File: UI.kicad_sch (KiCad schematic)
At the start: 40 parts

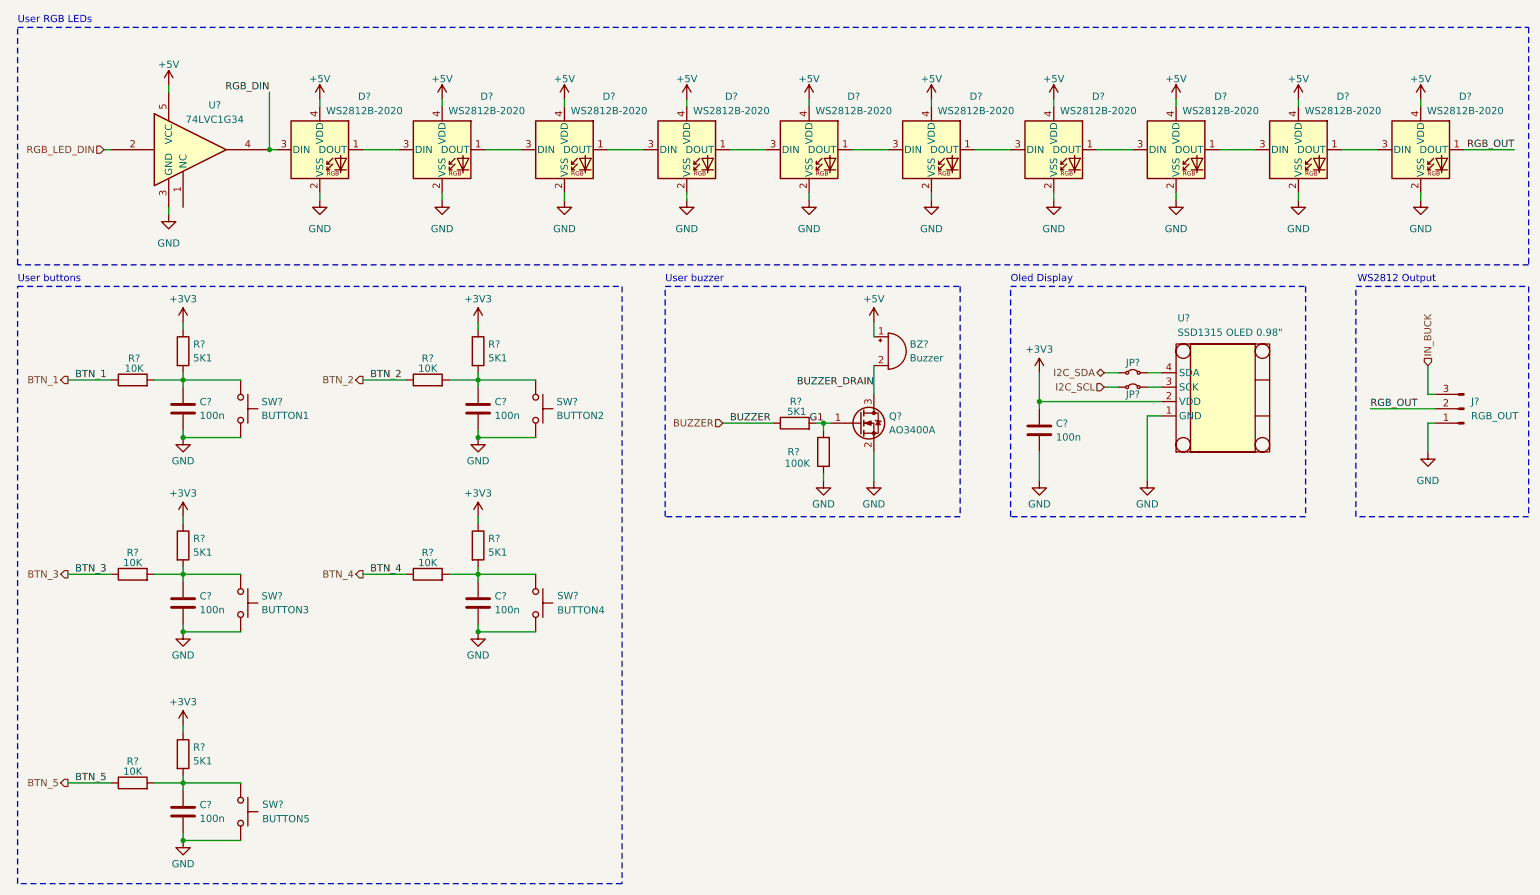
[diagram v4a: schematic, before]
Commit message: Referenced the shematic and started the sourcing part
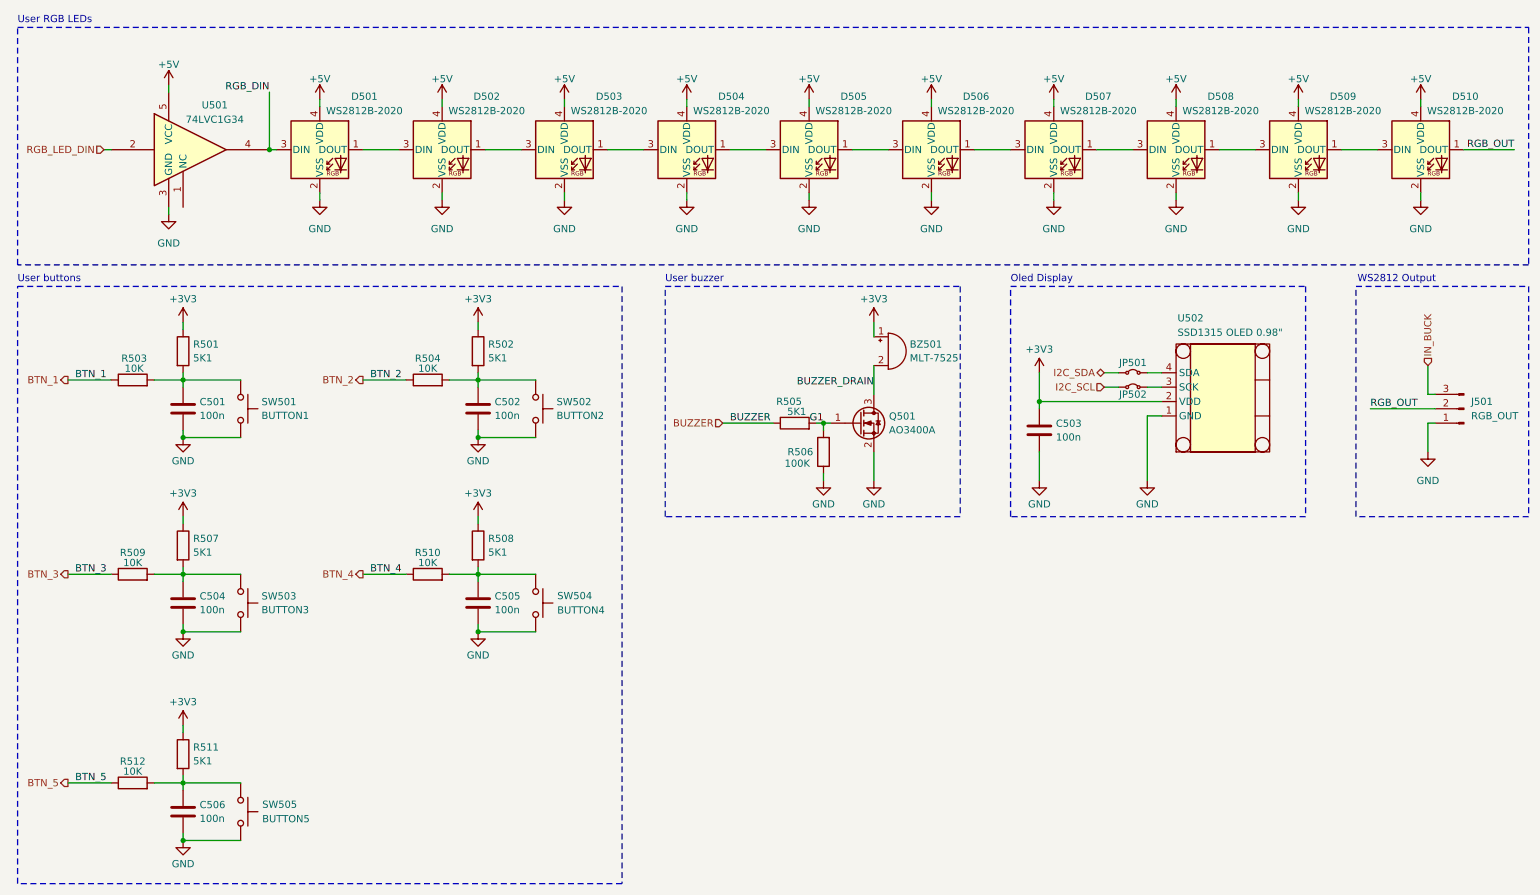
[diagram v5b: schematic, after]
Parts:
- BZ501: renamed from BZ?; value Buzzer -> MLT-7525; footprint Buzzer_Beeper:Buzzer_12x9.5RM7.6 -> (none); LCSC (none) -> C95299
- C501, C502, C503, C504, C505, C506: renamed from C?; footprint Capacitor_SMD:C_0805_2012Metric_Pad1.18x1.45mm_HandSolder -> Capacitor_SMD:C_0603_1608Metric_Pad1.08x0.95mm_HandSolder; LCSC (none) -> C14663
- J501: renamed from J?; footprint (none) -> Connector_PinHeader_2.54mm:PinHeader_1x03_P2.54mm_Vertical; LCSC (none) -> C492402
- R501, R502, R505, R507, R508, R511: renamed from R?; footprint Resistor_SMD:R_0805_2012Metric_Pad1.20x1.40mm_HandSolder -> Resistor_SMD:R_0603_1608Metric_Pad0.98x0.95mm_HandSolder; LCSC (none) -> C23186
- R503, R504, R509, R510, R512: renamed from R?; footprint Resistor_SMD:R_0805_2012Metric_Pad1.20x1.40mm_HandSolder -> Resistor_SMD:R_0603_1608Metric_Pad0.98x0.95mm_HandSolder; LCSC (none) -> C25804
- R506: renamed from R?; footprint Resistor_SMD:R_0805_2012Metric_Pad1.20x1.40mm_HandSolder -> Resistor_SMD:R_0603_1608Metric_Pad0.98x0.95mm_HandSolder; LCSC (none) -> C25803
- U502: renamed from U?; footprint (none) -> Connector_PinHeader_1.00mm:PinHeader_1x04_P1.00mm_Vertical; LCSC (none) -> C5248080
- gave numbers to parts that had none: 19
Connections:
- net +3V3: now also BZ501.1 (+)
- net +5V: no longer BZ501.1 (+)

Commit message: added some lcsc codes, changed reverse voltage protection with a diode
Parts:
- JP501, JP502: footprint (none) -> Resistor_SMD:R_0603_1608Metric_Pad0.98x0.95mm_HandSolder; LCSC (none) -> C21189
- Q501: LCSC (none) -> C5380685
- SW501, SW502, SW503, SW504, SW505: footprint Button_Switch_SMD:SW_SPST_SKQG_WithoutStem -> Button_Switch_SMD:SW_Push_1P1T_NO_CK_PTS125Sx43SMTR; LCSC (none) -> C455223

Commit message: added some lcsc PN, and uniformed some resistors values to reduce BOM count
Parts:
- R505: value 5K1 -> 560; LCSC C23186 -> C23204
- R506: value 100K -> 10K; LCSC C25803 -> C25804
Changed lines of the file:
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@@
 			)
 		)
-		(property "Value" "5K1"
+		(property "Value" "560"
 			(at 154.432 84.328 90)
 			(effects
@@
 			)
 		)
-		(property "LCSC" "C23186"
+		(property "LCSC" "C23204"
 			(at 152.4 86.36 90)
 			(effects
@@
 			)
 		)
-		(property "Value" "100K"
+		(property "Value" "10K"
 			(at 150.622 93.472 0)
 			(effects
@@
 			)
 		)
-		(property "LCSC" "C25803"
+		(property "LCSC" "C25804"
 			(at 157.48 91.44 0)
 			(effects

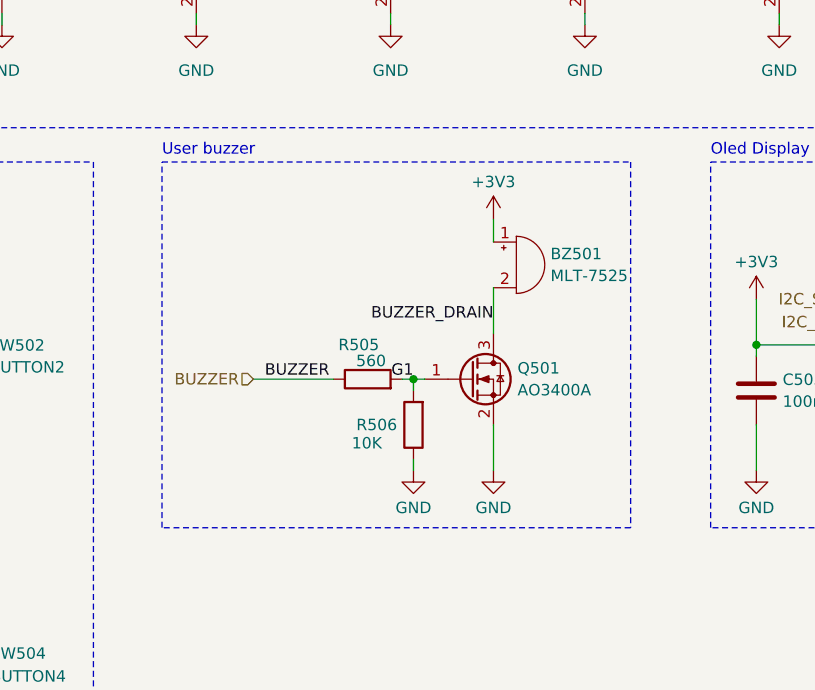
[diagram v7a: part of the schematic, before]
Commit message: Created buzzer footprint, and fixed some libraries simbols and footprint
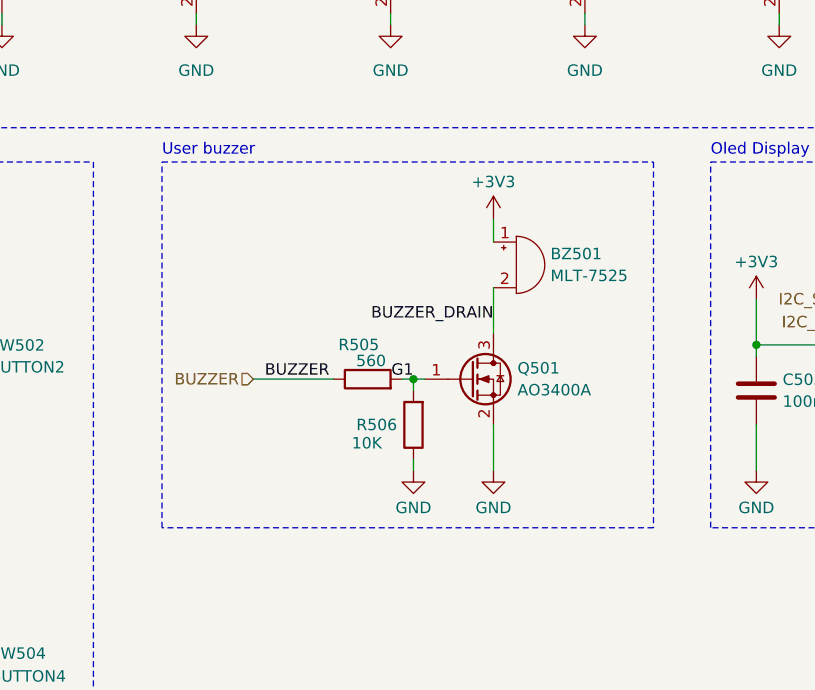
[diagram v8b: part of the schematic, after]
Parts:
- BZ501: footprint (none) -> ProjectConnectors:Buzzer MLT-7525
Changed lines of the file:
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@@
 	(rectangle
 		(start 129.54 62.23)
-		(end 181.61 102.87)
+		(end 184.15 102.87)
 		(stroke
 			(width 0)
@@
 			)
 		)
-		(property "Footprint" ""
+		(property "Footprint" "ProjectConnectors:Buzzer MLT-7525"
 			(at 168.275 71.12 90)
 			(effects
